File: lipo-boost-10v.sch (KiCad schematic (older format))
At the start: 1 part

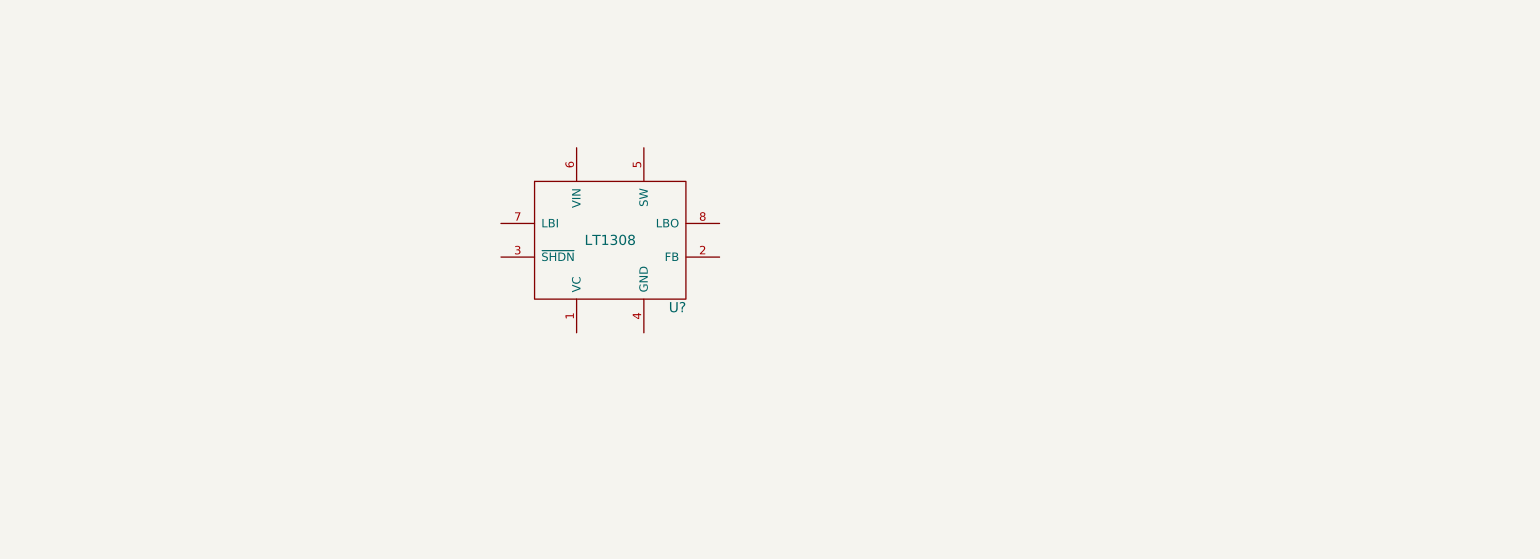
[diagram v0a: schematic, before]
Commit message: Add lithium cell to 10v boost circuit
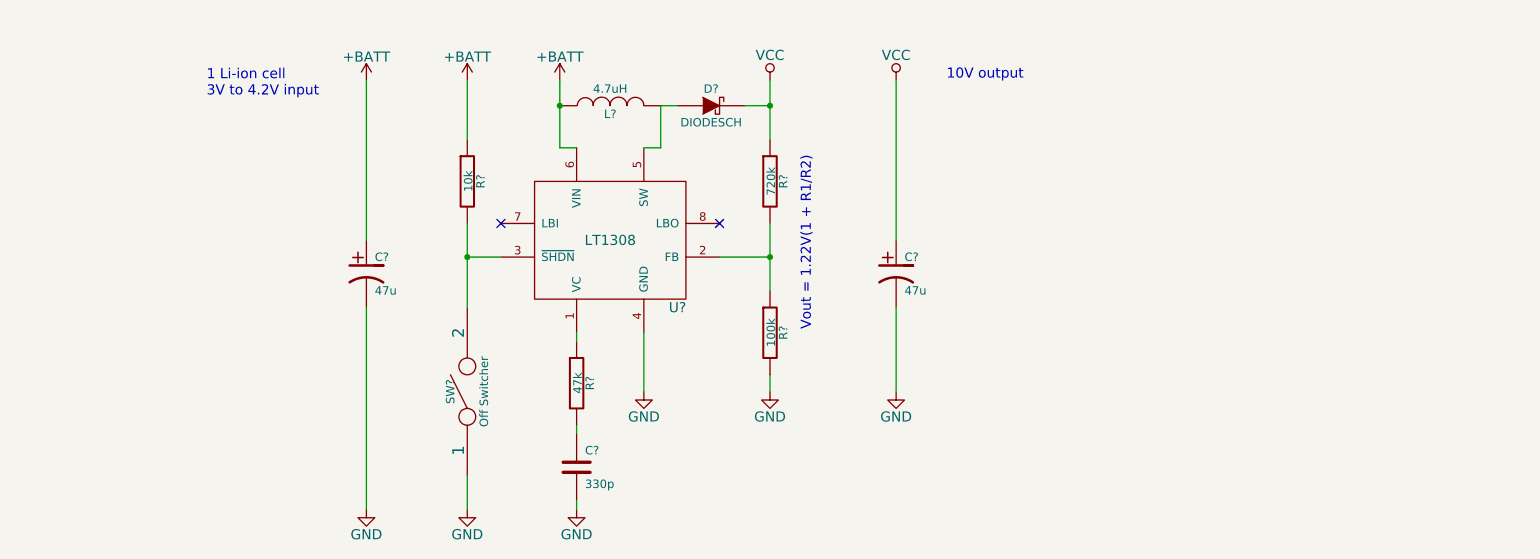
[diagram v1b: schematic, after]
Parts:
- added C?: 330p, symbol C
- added C? (x2): 47u, symbol CP1
- added D?: DIODESCH, symbol DIODESCH
- added L?: 4.7uH, symbol INDUCTOR
- added R?: 47k, symbol R
- added R?: 10k, symbol R
- added R?: 720k, symbol R
- added R?: 100k, symbol R
- added SW?: Off Switcher, symbol SPST
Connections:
- net at U?.1 (VC): now also R?.1
- net at U?.2 (FB): now also R?.1, R?.2
- net at U?.3 (~SHDN): now also R?.2, SW?.2
- net GND: now reaches U?.4 (GND)
- net GND: now also C?.2, C?.2, C?.2, R?.2, SW?.1
- net at U?.5 (SW): now also D?.1 (A), L?.2
- net +BATT: now reaches U?.6 (VIN)
- net +BATT: now also C?.1, L?.1, R?.1
- new net: C?.1, R?.2
- new net VCC: C?.1, D?.2 (K), R?.1
- no-connect marks 0 -> 2
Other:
- note added: "1 Li-ion cell\n3V to 4.2V input"
- note added: "10V output"
- note added: "Vout = 1.22V(1 + R1/R2)"

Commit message: Add low-battery detection stage
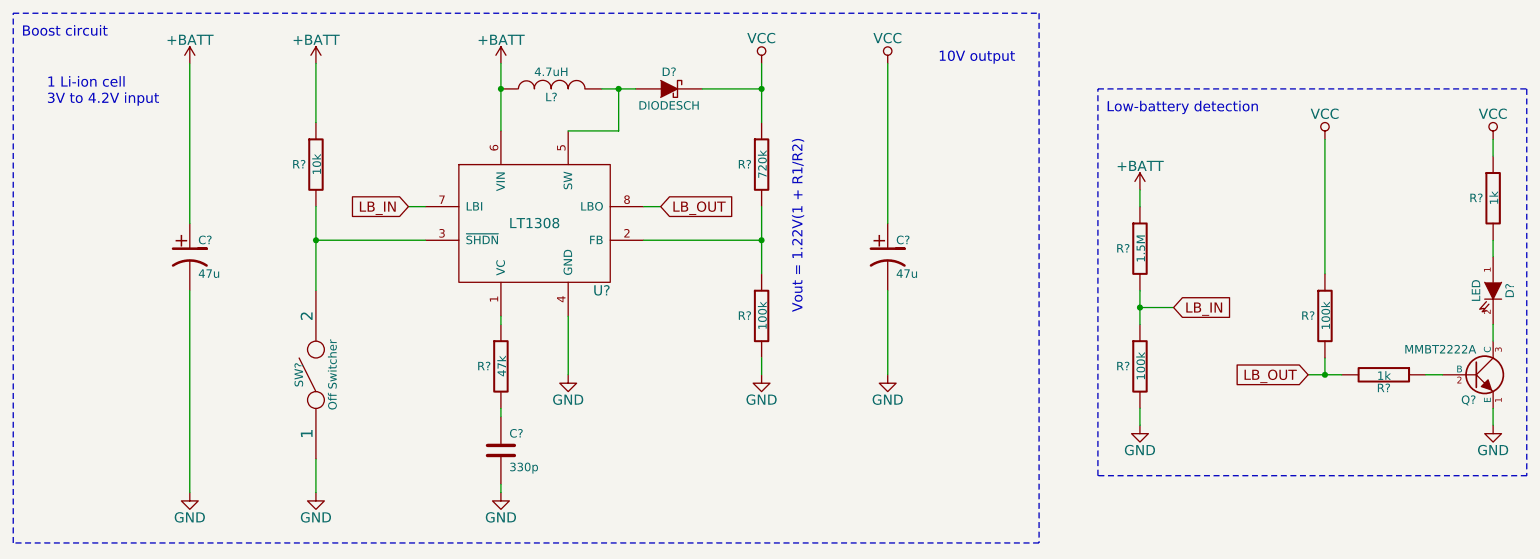
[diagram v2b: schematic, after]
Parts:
- added D?: LED, symbol LED
- added Q?: MMBT2222A, symbol NPN
- added R?: 1.5M, symbol R
- added R? (x2): 100k, symbol R
- added R? (x2): 1k, symbol R
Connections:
- net +BATT: now also R?.1
- net GND: now also Q?.1 (E), R?.2
- net VCC: now also R?.1, R?.1
- net LB_IN: now reaches U?.7 (LBI)
- net LB_IN: now also R?.1, R?.2
- net LB_OUT: now reaches U?.8 (LBO)
- net LB_OUT: now also R?.2, R?.2
- new net: Q?.2 (B), R?.1
- new net: D?.2 (K), Q?.3 (C)
- new net: D?.1 (A), R?.2
- no-connect marks 2 -> 0
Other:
- note added: "Boost circuit"
- note added: "Low-battery detection"
- moved on the sheet: C?, D?, L?, R?, SW?, U?

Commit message: Correct value of a resistor & Generate netlist
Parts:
- R20: renamed from R?; value 1k -> 470
- gave numbers to parts that had none: 17
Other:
- moved on the sheet: R22
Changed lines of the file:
@@
 $EndDescr
 $Comp
-L LT1308 U?
+L LT1308 U4
 U 1 1 54D15AD0
 P 4450 3400
-F 0 "U?" H 4850 3050 60  0000 C CNN
+F 0 "U4" H 4850 3050 60  0000 C CNN
 F 1 "LT1308" H 4450 3450 60  0000 C CNN
 F 2 "" H 4500 3400 60  0000 C CNN
@@
 $EndComp
 $Comp
-L R R?
+L R R24
 U 1 1 54D20F41
 P 4250 4200
-F 0 "R?" H 4150 4200 50  0000 C CNN
+F 0 "R24" H 4100 4200 50  0000 C CNN
 F 1 "47k" V 4257 4201 50  0000 C CNN
 F 2 "" V 4180 4200 30  0000 C CNN
@@
 $EndComp
 $Comp
-L C C?
+L C C11
 U 1 1 54D20F86
 P 4250 4700
-F 0 "C?" H 4300 4800 50  0000 L CNN
+F 0 "C11" H 4300 4800 50  0000 L CNN
 F 1 "330p" H 4300 4600 50  0000 L CNN
 F 2 "" H 4288 4550 30  0000 C CNN
@@
 $EndComp
 $Comp
-L GND #PWR?
+L GND #PWR026
 U 1 1 54D21030
 P 4250 4950
-F 0 "#PWR?" H 4250 4700 60  0001 C CNN
+F 0 "#PWR026" H 4250 4700 60  0001 C CNN
 F 1 "GND" H 4250 4800 60  0000 C CNN
 F 2 "" H 4250 4950 60  0000 C CNN
@@
 $EndComp
 $Comp
-L GND #PWR?
+L GND #PWR027
 U 1 1 54D21045
 P 4650 4250
-F 0 "#PWR?" H 4650 4000 60  0001 C CNN
+F 0 "#PWR027" H 4650 4000 60  0001 C CNN
 F 1 "GND" H 4650 4100 60  0000 C CNN
 F 2 "" H 4650 4250 60  0000 C CNN
@@
 	4250 4900 4250 4950
 $Comp
-L R R?
+L R R18
 U 1 1 54D21070
 P 3150 3000
-F 0 "R?" H 3050 3000 50  0000 C CNN
+F 0 "R18" H 3000 3000 50  0000 C CNN
 F 1 "10k" V 3157 3001 50  0000 C CNN
 F 2 "" V 3080 3000 30  0000 C CNN
@@
 $EndComp
 $Comp
-L SPST SW?
+L SPST SW1
 U 1 1 54D210CF
 P 3150 4250
-F 0 "SW?" H 3150 4350 50  0000 C CNN
+F 0 "SW1" V 3150 4400 50  0000 C CNN
 F 1 "Off Switcher" H 3150 4150 50  0000 C CNN
 F 2 "" H 3150 4250 60  0000 C CNN
@@
 Connection ~ 3150 3450
 $Comp
-L +BATT #PWR?
+L +BATT #PWR028
 U 1 1 54D21149
 P 3150 2400
-F 0 "#PWR?" H 3150 2250 60  0001 C CNN
+F 0 "#PWR028" H 3150 2250 60  0001 C CNN
 F 1 "+BATT" H 3150 2540 60  0000 C CNN
 F 2 "" H 3150 2400 60  0000 C CNN
@@
 	3150 2400 3150 2750
 $Comp
-L GND #PWR?
+L GND #PWR029
 U 1 1 54D21567
 P 3150 4950
-F 0 "#PWR?" H 3150 4700 60  0001 C CNN
+F 0 "#PWR029" H 3150 4700 60  0001 C CNN
 F 1 "GND" H 3150 4800 60  0000 C CNN
 F 2 "" H 3150 4950 60  0000 C CNN
@@
 	3150 4950 3150 4750
 $Comp
-L INDUCTOR L?
+L INDUCTOR L1
 U 1 1 54D215CE
 P 4550 2550
-F 0 "L?" V 4500 2550 50  0000 C CNN
+F 0 "L1" V 4500 2550 50  0000 C CNN
 F 1 "4.7uH" V 4650 2550 50  0000 C CNN
 F 2 "" H 4550 2550 60  0000 C CNN
@@
 	4650 2800 4950 2800
 $Comp
-L DIODESCH D?
+L DIODESCH D6
 U 1 1 54D2162D
 P 5250 2550
-F 0 "D?" H 5250 2650 50  0000 C CNN
+F 0 "D6" H 5250 2650 50  0000 C CNN
 F 1 "DIODESCH" H 5250 2450 50  0000 C CNN
 F 2 "" H 5250 2550 60  0000 C CNN
@@
 	4850 2550 5050 2550
 $Comp
-L R R?
+L R R19
 U 1 1 54D21668
 P 5800 3000
-F 0 "R?" H 5700 3000 50  0000 C CNN
+F 0 "R19" H 5650 3000 50  0000 C CNN
 F 1 "720k" V 5807 3001 50  0000 C CNN
 F 2 "" V 5730 3000 30  0000 C CNN
@@
 $EndComp
 $Comp
-L R R?
+L R R23
 U 1 1 54D21691
 P 5800 3900
-F 0 "R?" H 5700 3900 50  0000 C CNN
+F 0 "R23" H 5650 3900 50  0000 C CNN
 F 1 "100k" V 5807 3901 50  0000 C CNN
 F 2 "" V 5730 3900 30  0000 C CNN
@@
 	5800 2550 5450 2550
 $Comp
-L +BATT #PWR?
+L +BATT #PWR030
 U 1 1 54D21743
 P 4250 2400
-F 0 "#PWR?" H 4250 2250 60  0001 C CNN
+F 0 "#PWR030" H 4250 2250 60  0001 C CNN
 F 1 "+BATT" H 4250 2540 60  0000 C CNN
 F 2 "" H 4250 2400 60  0000 C CNN
@@
 Vout = 1.22V(1 + R1/R2)
 $Comp
-L GND #PWR?
+L GND #PWR031
 U 1 1 54D21E39
 P 5800 4250
-F 0 "#PWR?" H 5800 4000 60  0001 C CNN
+F 0 "#PWR031" H 5800 4000 60  0001 C CNN
 F 1 "GND" H 5800 4100 60  0000 C CNN
 F 2 "" H 5800 4250 60  0000 C CNN
@@
 	5800 4250 5800 4150
 $Comp
-L +BATT #PWR?
+L +BATT #PWR032
 U 1 1 54D22EEE
 P 2400 2400
-F 0 "#PWR?" H 2400 2250 60  0001 C CNN
+F 0 "#PWR032" H 2400 2250 60  0001 C CNN
 F 1 "+BATT" H 2400 2540 60  0000 C CNN
 F 2 "" H 2400 2400 60  0000 C CNN
@@
 $EndComp
 $Comp
-L GND #PWR?
+L GND #PWR033
 U 1 1 54D22F02
 P 2400 4950
-F 0 "#PWR?" H 2400 4700 60  0001 C CNN
+F 0 "#PWR033" H 2400 4700 60  0001 C CNN
 F 1 "GND" H 2400 4800 60  0000 C CNN
 F 2 "" H 2400 4950 60  0000 C CNN
@@
 $EndComp
 $Comp
-L CP1 C?
+L CP1 C9
 U 1 1 54D22F0F
 P 2400 3550
-F 0 "C?" H 2450 3650 50  0000 L CNN
+F 0 "C9" H 2450 3650 50  0000 L CNN
 F 1 "47u" H 2450 3450 50  0000 L CNN
 F 2 "" H 2400 3550 60  0000 C CNN
@@
 	2400 3750 2400 4950
 $Comp
-L GND #PWR?
+L GND #PWR034
 U 1 1 54D234B6
 P 6550 4250
-F 0 "#PWR?" H 6550 4000 60  0001 C CNN
+F 0 "#PWR034" H 6550 4000 60  0001 C CNN
 F 1 "GND" H 6550 4100 60  0000 C CNN
 F 2 "" H 6550 4250 60  0000 C CNN
@@
 $EndComp
 $Comp
-L CP1 C?
+L CP1 C10
 U 1 1 54D234BC
 P 6550 3550
-F 0 "C?" H 6600 3650 50  0000 L CNN
+F 0 "C10" H 6600 3650 50  0000 L CNN
 F 1 "47u" H 6600 3450 50  0000 L CNN
 F 2 "" H 6550 3550 60  0000 C CNN
@@
 10V output
 $Comp
-L VCC #PWR?
+L VCC #PWR035
 U 1 1 54D23651
 P 5800 2400
-F 0 "#PWR?" H 5800 2250 60  0001 C CNN
+F 0 "#PWR035" H 5800 2250 60  0001 C CNN
 F 1 "VCC" H 5800 2550 60  0000 C CNN
 F 2 "" H 5800 2400 60  0000 C CNN
@@
 $EndComp
 $Comp
-L VCC #PWR?
+L VCC #PWR036
 U 1 1 54D2366E
 P 6550 2400
-F 0 "#PWR?" H 6550 2250 60  0001 C CNN
+F 0 "#PWR036" H 6550 2250 60  0001 C CNN
 F 1 "VCC" H 6550 2550 60  0000 C CNN
 F 2 "" H 6550 2400 60  0000 C CNN
@@
 LB_OUT
 $Comp
-L GND #PWR?
+L GND #PWR037
 U 1 1 54D26E5B
 P 8050 4550
-F 0 "#PWR?" H 8050 4300 60  0001 C CNN
+F 0 "#PWR037" H 8050 4300 60  0001 C CNN
 F 1 "GND" H 8050 4400 60  0000 C CNN
 F 2 "" H 8050 4550 60  0000 C CNN
@@
 $EndComp
 $Comp
-L VCC #PWR?
+L VCC #PWR038
 U 1 1 54D26E71
-P 9150 2850
-F 0 "#PWR?" H 9150 2700 60  0001 C CNN
-F 1 "VCC" H 9150 3000 60  0000 C CNN
-F 2 "" H 9150 2850 60  0000 C CNN
-F 3 "" H 9150 2850 60  0000 C CNN
-	1    9150 2850
-	1    0    0    -1
-$EndComp
-$Comp
-L GND #PWR?
+P 9150 3150
+F 0 "#PWR038" H 9150 3000 60  0001 C CNN
+F 1 "VCC" H 9150 3300 60  0000 C CNN
+F 2 "" H 9150 3150 60  0000 C CNN
+F 3 "" H 9150 3150 60  0000 C CNN
+	1    9150 3150
+	1    0    0    -1
+$EndComp
+$Comp
+L GND #PWR039
 U 1 1 54D26E92
 P 10150 4550
-F 0 "#PWR?" H 10150 4300 60  0001 C CNN
+F 0 "#PWR039" H 10150 4300 60  0001 C CNN
 F 1 "GND" H 10150 4400 60  0000 C CNN
 F 2 "" H 10150 4550 60  0000 C CNN
@@
 $EndComp
 $Comp
-L R R?
+L R R21
 U 1 1 54D26ED6
 P 8050 3500
-F 0 "R?" H 7950 3500 50  0000 C CNN
+F 0 "R21" H 7900 3500 50  0000 C CNN
 F 1 "1.5M" V 8057 3501 50  0000 C CNN
 F 2 "" V 7980 3500 30  0000 C CNN
@@
 $EndComp
 $Comp
-L +BATT #PWR?
+L +BATT #PWR040
 U 1 1 54D26F23
 P 8050 3150
-F 0 "#PWR?" H 8050 3000 60  0001 C CNN
+F 0 "#PWR040" H 8050 3000 60  0001 C CNN
 F 1 "+BATT" H 8050 3290 60  0000 C CNN
 F 2 "" H 8050 3150 60  0000 C CNN
@@
 $EndComp
 $Comp
-L R R?
+L R R25
 U 1 1 54D26F7B
 P 8050 4200
-F 0 "R?" H 7950 4200 50  0000 C CNN
+F 0 "R25" H 7900 4200 50  0000 C CNN
 F 1 "100k" V 8057 4201 50  0000 C CNN
 F 2 "" V 7980 4200 30  0000 C CNN
@@
 Connection ~ 8050 3850
 $Comp
-L R R?
+L R R22
 U 1 1 54D27112
-P 9150 3900
-F 0 "R?" H 9050 3900 50  0000 C CNN
-F 1 "100k" V 9157 3901 50  0000 C CNN
-F 2 "" V 9080 3900 30  0000 C CNN
-F 3 "" H 9150 3900 30  0000 C CNN
-	1    9150 3900
-	1    0    0    -1
-$EndComp
-Wire Wire Line
-	9150 2850 9150 3650
-$Comp
-L R R?
+P 9150 3500
+F 0 "R22" H 9000 3500 50  0000 C CNN
+F 1 "100k" V 9157 3501 50  0000 C CNN
+F 2 "" V 9080 3500 30  0000 C CNN
+F 3 "" H 9150 3500 30  0000 C CNN
+	1    9150 3500
+	1    0    0    -1
+$EndComp
+Wire Wire Line
+	9150 3150 9150 3250
+$Comp
+L R R26
 U 1 1 54D271FC
 P 9500 4250
-F 0 "R?" V 9580 4250 50  0000 C CNN
+F 0 "R26" V 9580 4250 50  0000 C CNN
 F 1 "1k" V 9507 4251 50  0000 C CNN
 F 2 "" V 9430 4250 30  0000 C CNN
@@
 $EndComp
 Wire Wire Line
-	9150 4150 9150 4250
+	9150 3750 9150 4250
 Wire Wire Line
 	9050 4250 9250 4250
 Connection ~ 9150 4250
 $Comp
-L NPN Q?
+L NPN Q3
 U 1 1 54D277B4
 P 10050 4250
-F 0 "Q?" H 10050 4100 50  0000 R CNN
+F 0 "Q3" H 10050 4100 50  0000 R CNN
 F 1 "MMBT2222A" H 10050 4400 50  0000 R CNN
 F 2 "" H 10050 4250 60  0000 C CNN
@@
 	10150 4550 10150 4450
 $Comp
-L R R?
+L R R20
 U 1 1 54D278E2
 P 10150 3200
-F 0 "R?" H 10050 3200 50  0000 C CNN
-F 1 "1k" V 10157 3201 50  0000 C CNN
+F 0 "R20" H 10000 3200 50  0000 C CNN
+F 1 "470" V 10157 3201 50  0000 C CNN
 F 2 "" V 10080 3200 30  0000 C CNN
 F 3 "" H 10150 3200 30  0000 C CNN
@@
 $EndComp
 $Comp
-L LED D?
+L LED D7
 U 1 1 54D27932
 P 10150 3750
-F 0 "D?" H 10150 3850 50  0000 C CNN
+F 0 "D7" H 10150 3850 50  0000 C CNN
 F 1 "LED" H 10150 3650 50  0000 C CNN
 F 2 "" H 10150 3750 60  0000 C CNN
@@
 	10150 3550 10150 3450
 $Comp
-L VCC #PWR?
+L VCC #PWR041
 U 1 1 54D27A03
 P 10150 2850
-F 0 "#PWR?" H 10150 2700 60  0001 C CNN
+F 0 "#PWR041" H 10150 2700 60  0001 C CNN
 F 1 "VCC" H 10150 3000 60  0000 C CNN
 F 2 "" H 10150 2850 60  0000 C CNN

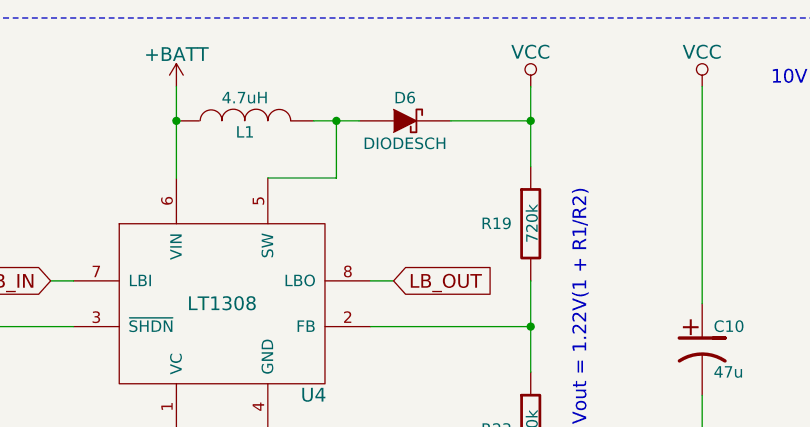
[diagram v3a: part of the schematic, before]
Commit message: Associate footprints to components
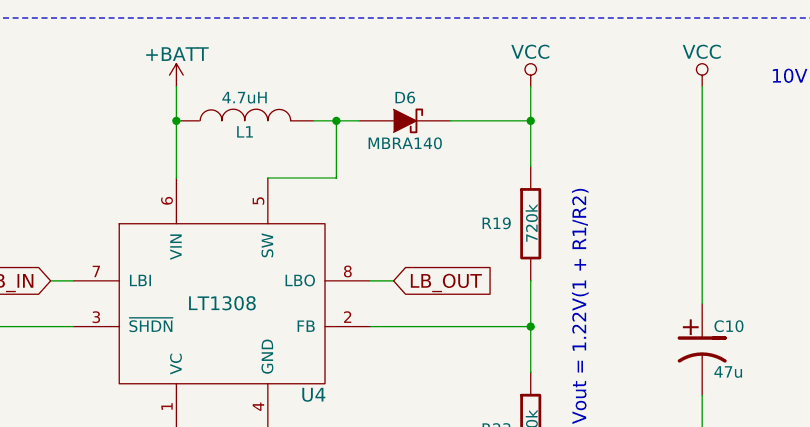
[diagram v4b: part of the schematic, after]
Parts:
- D6: value DIODESCH -> MBRA140
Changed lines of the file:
@@
 P 5250 2550
 F 0 "D6" H 5250 2650 50  0000 C CNN
-F 1 "DIODESCH" H 5250 2450 50  0000 C CNN
+F 1 "MBRA140" H 5250 2450 50  0000 C CNN
 F 2 "" H 5250 2550 60  0000 C CNN
 F 3 "" H 5250 2550 60  0000 C CNN
